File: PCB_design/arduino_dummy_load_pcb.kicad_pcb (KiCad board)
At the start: 2 copper layers, 122 parts, among them J1 Barrel_Jack, J2 Conn_02x08_Odd_Even, U1 MCP3208

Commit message: KiCad routing for the win!
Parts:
- removed the QB1 at (210.8, 87.6)
- moved BATT2 308.3 mm to (312.4, 160.0)
- moved RB4 212.4 mm to (266.6, 115.6)
- moved RB8 212.1 mm to (266.8, 125.7)
- moved DB2 207.4 mm to (273.9, 119.4)
- moved RB7 205.1 mm to (266.7, 120.7)
- moved BATT1 190.4 mm to (157.5, 142.2), turned to 270 degrees
- moved DB1 190.3 mm to (256.5, 114.3)
- moved DB4 190.3 mm to (256.5, 121.9)
- moved DB5 190.3 mm to (256.5, 124.5)
- moved RB5 183.1 mm to (248.9, 72.4)
- moved DB3 181.4 mm to (252.7, 103.8), turned to 90 degrees
- moved RB6 179.0 mm to (248.8, 77.5)
- moved RB3 170.5 mm to (248.8, 82.5)
- moved CB4 154.8 mm to (227.3, 96.5), turned to 90 degrees
- moved QA4 136.3 mm to (160.0, 106.7), turned to 180 degrees
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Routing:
- net GND: track 4.77 -> 160.5 mm
- net Net-(QA2-Pad3): track 0.00 -> 126.9 mm
- net Net-(QA3-Pad3): track 0.00 -> 115.0 mm
- net Net-(CA2-Pad1): track 10.3 -> 44.4 mm
- net I_OUT_A: track 0.00 -> 26.7 mm
- net Net-(QA2-Pad1): track 0.00 -> 24.2 mm
- net Net-(QA3-Pad1): track 0.00 -> 18.6 mm
- net Net-(DA1-Pad1): track 0.00 -> 18.5 mm
- net Net-(CA4-Pad1): track 0.00 -> 15.8 mm
- net Net-(CA3-Pad1): track 0.00 -> 14.6 mm
- net Net-(DA2-Pad1): track 0.00 -> 13.5 mm
- net /TEST-UNIT-A/STOP: track 0.00 -> 12.0 mm
- net VREF: track 10.4 -> 21.6 mm
- net +5V: track 21.2 -> 31.6 mm
- net Net-(DA3-Pad1): track 0.00 -> 5.63 mm
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
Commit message: nearly finished PCB layout and routing
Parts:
- removed BATT2: Battery_Cell, Library:18650
- removed CB1, CB2: 10uF, Capacitors_SMD:C_0805_HandSoldering
- removed CB3, CB4: 100nF, Capacitors_SMD:C_0805_HandSoldering
- removed DB1, DB2, DB3, DB4, DB5: D, Diodes_SMD:D_SOD-123
- removed QB1, QB4: IPP45P03P4L-11, TO_SOT_Packages_THT:TO-220-3_Vertical
- removed QB2, QB3: IRFZ44N, TO_SOT_Packages_THT:TO-220-3_Vertical
- removed R10, R11, R12, R13, R14, R8, R9, RB2, RB3, RB4, RB5, RB6, RB7, RB8: 47k, Resistors_SMD:R_0805_HandSoldering
- removed RB1: 50m, Resistors_SMD:R_2512_HandSoldering
- removed RB10, RB9: POT, Potentiometers:Potentiometer_Trimmer_ACP_CA6v_Horizontal_MountLS
- removed RB11: 10k, Resistors_SMD:R_0805_HandSoldering
- removed RSB1, RSB10, RSB11, RSB12, RSB13, RSB14, RSB15, RSB16, RSB17, RSB18, RSB19, RSB2, RSB20, RSB3, RSB4, RSB5, RSB6, RSB7, RSB8, RSB9: 10, Resistors_THT:R_Axial_DIN0617_L17.0mm_D6.0mm_P7.62mm_Vertical
- removed UB1: MCP73826, TO_SOT_Packages_SMD:SOT-23-6_Handsoldering
- removed UB2: LM324, Housings_SOIC:SOIC-14_3.9x8.7mm_Pitch1.27mm
- removed UB3, UB4, UB5: TMP36, TO_SOT_Packages_THT:TO-92_Inline_Wide
- RA10, RA9: footprint Potentiometers:Potentiometer_Trimmer_ACP_CA6v_Horizontal_MountLS -> Potentiometers:Potentiometer_Trimmer_VishaySpectrol_Econtrim-Type36M
- moved J1 88.8 mm to (64.5, 119.4)
- moved RA6 81.6 mm to (78.7, 128.2), turned to 270 degrees
- moved R3 69.3 mm to (73.7, 128.2), turned to 270 degrees
- moved UA5 68.7 mm to (143.5, 120.7), turned to 270 degrees
- moved RA3 65.7 mm to (76.2, 128.2), turned to 270 degrees
- moved R4 61.1 mm to (71.1, 128.2)
- moved DA4 61.0 mm to (141.0, 116.8), turned to 0 degrees
- moved R1 56.9 mm to (82.5, 92.7)
- moved R2 56.8 mm to (82.5, 95.2)
- moved R5 52.2 mm to (82.5, 102.9), turned to 0 degrees
- moved J2 50.6 mm to (74.9, 83.8), turned to 180 degrees
- moved R7 50.1 mm to (82.5, 97.8), turned to 0 degrees
- moved R6 44.7 mm to (82.6, 100.3), turned to 0 degrees
- moved U1 37.3 mm to (73.8, 101.8), turned to 180 degrees
- moved DA3 37.2 mm to (110.1, 111.8), turned to 180 degrees
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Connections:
- R4 pad 1: Net-(R3-Pad1) -> Net-(R4-Pad1)
- R4 pad 2: GND -> CELL_TEMP_A
- R5 pad 2: I_OUT_A -> BATT_B
- R6 pad 1: Net-(R5-Pad1) -> Net-(R6-Pad1)
- R6 pad 2: GND -> I_OUT_B
- R7 pad 2: CELL_TEMP_A -> CELL_TEMP_B
- U1 pad 2: Net-(R5-Pad1) -> I_OUT_A
- U1 pad 3: Net-(R7-Pad1) -> Net-(R4-Pad1)
- U1 pad 4: Net-(R10-Pad1) -> Net-(R5-Pad1)
- U1 pad 5: Net-(R11-Pad1) -> Net-(R6-Pad1)
- U1 pad 6: Net-(R13-Pad1) -> Net-(R7-Pad1)
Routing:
- net BATT_A: track 5.08 -> 146.5 mm
- net CELL_TEMP_A: track 0.00 -> 88.2 mm
- net CHARGE: track 5.72 -> 83.8 mm
- net +9V: track 0.00 -> 67.9 mm
- net Net-(QA3-Pad3): track 115.0 -> 171.5 mm
- net I_SET: track 3.96 -> 50.0 mm
- net Net-(QA2-Pad3): track 126.9 -> 168.4 mm
- net GND: track 160.5 -> 119.9 mm
- net Net-(CA2-Pad1): track 44.4 -> 81.6 mm
- net Net-(DA3-Pad1): track 5.63 -> 40.0 mm
- net Net-(DA3-Pad2): track 0.00 -> 30.1 mm
- net Net-(R4-Pad1): track 0.00 -> 25.7 mm
- net Net-(QB1-Pad3): track 15.4 -> 0.00 mm
- net Net-(R13-Pad1): track 13.4 -> 0.00 mm
- net Net-(R11-Pad1): track 13.0 -> 0.00 mm
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
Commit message: Finalized/finished PCB layout. Phew! Version 0.00. Hopefully it works (fingers crossed)!
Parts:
- removed R7: 47k, Resistors_SMD:R_0805_HandSoldering
- added BATT2: Battery_Cell, Library:18650, F.Cu at (255.3, 111.8)
- added CB1: 10uF, Capacitors_SMD:C_0805_HandSoldering, F.Cu at (247.7, 59.7)
- added CB2: 10uF, Capacitors_SMD:C_0805_HandSoldering, F.Cu at (254.0, 68.6)
- added CB3: 100nF, Capacitors_SMD:C_0805_HandSoldering, F.Cu at (218.6, 64.8)
- added CB4: 100nF, Capacitors_SMD:C_0805_HandSoldering, F.Cu at (213.7, 64.8)
- added DB1: D, Diodes_SMD:D_SOD-123, F.Cu at (210.6, 76.6)
- added DB2: D, Diodes_SMD:D_SOD-123, F.Cu at (219.3, 85.2)
- added DB3: D, Diodes_SMD:D_SOD-123, F.Cu at (213.0, 69.8)
- added DB4: D, Diodes_SMD:D_SOD-123, F.Cu at (243.8, 74.9)
- added DB5: D, Diodes_SMD:D_SOD-123, F.Cu at (220.4, 69.8)
- added QB1: IPP45P03P4L-11, TO_SOT_Packages_THT:TO-220-3_Vertical, F.Cu at (258.0, 64.3)
- added QB2: IRFZ44N, TO_SOT_Packages_THT:TO-220-3_Vertical, F.Cu at (191.8, 77.5)
- added QB3: IRFZ44N, TO_SOT_Packages_THT:TO-220-3_Vertical, F.Cu at (238.8, 77.5)
- added QB4: IPP45P03P4L-11, TO_SOT_Packages_THT:TO-220-3_Vertical, F.Cu at (257.8, 76.2)
- added RB1: 50m, Resistors_SMD:R_2512_HandSoldering, F.Cu at (244.2, 64.3)
- added RB10: POT, Potentiometers:Potentiometer_Trimmer_VishaySpectrol_Econtrim-Type36M, F.Cu at (214.6, 57.2)
- added RB11: 10k, Resistors_SMD:R_0805_HandSoldering, F.Cu at (217.0, 68.8)
- added RB2: 47k, Resistors_SMD:R_0805_HandSoldering, F.Cu at (252.7, 59.7)
- added RB3: 47k, Resistors_SMD:R_0805_HandSoldering, F.Cu at (179.1, 86.4)
- added RB4: 47k, Resistors_SMD:R_0805_HandSoldering, F.Cu at (215.9, 87.5)
- added RB5: 47k, Resistors_SMD:R_0805_HandSoldering, F.Cu at (210.6, 81.7)
- added RB6: 47k, Resistors_SMD:R_0805_HandSoldering, F.Cu at (181.6, 86.4)
- added RB7: 47k, Resistors_SMD:R_0805_HandSoldering, F.Cu at (224.9, 85.1)
- added RB8: 47k, Resistors_SMD:R_0805_HandSoldering, F.Cu at (226.0, 81.7)
- added RB9: POT, Potentiometers:Potentiometer_Trimmer_VishaySpectrol_Econtrim-Type36M, F.Cu at (223.5, 57.2)
- added REG1: REG, Library:LM2596_module, F.Cu at (79.3, 101.6)
- added RSB1: 10, Resistors_THT:R_Axial_DIN0617_L17.0mm_D6.0mm_P7.62mm_Vertical, F.Cu at (202.8, 130.7)
- added RSB10: 10, Resistors_THT:R_Axial_DIN0617_L17.0mm_D6.0mm_P7.62mm_Vertical, F.Cu at (215.5, 100.2)
- added RSB11: 10, Resistors_THT:R_Axial_DIN0617_L17.0mm_D6.0mm_P7.62mm_Vertical, F.Cu at (229.5, 130.7)
- added RSB12: 10, Resistors_THT:R_Axial_DIN0617_L17.0mm_D6.0mm_P7.62mm_Vertical, F.Cu at (229.5, 123.0)
- added RSB13: 10, Resistors_THT:R_Axial_DIN0617_L17.0mm_D6.0mm_P7.62mm_Vertical, F.Cu at (229.5, 115.4)
- added RSB14: 10, Resistors_THT:R_Axial_DIN0617_L17.0mm_D6.0mm_P7.62mm_Vertical, F.Cu at (229.5, 107.8)
- added RSB15: 10, Resistors_THT:R_Axial_DIN0617_L17.0mm_D6.0mm_P7.62mm_Vertical, F.Cu at (229.5, 100.2)
- added RSB16: 10, Resistors_THT:R_Axial_DIN0617_L17.0mm_D6.0mm_P7.62mm_Vertical, F.Cu at (242.2, 130.7)
- added RSB17: 10, Resistors_THT:R_Axial_DIN0617_L17.0mm_D6.0mm_P7.62mm_Vertical, F.Cu at (242.2, 123.0)
- added RSB18: 10, Resistors_THT:R_Axial_DIN0617_L17.0mm_D6.0mm_P7.62mm_Vertical, F.Cu at (242.2, 115.4)
- added RSB19: 10, Resistors_THT:R_Axial_DIN0617_L17.0mm_D6.0mm_P7.62mm_Vertical, F.Cu at (242.2, 107.8)
- added RSB2: 10, Resistors_THT:R_Axial_DIN0617_L17.0mm_D6.0mm_P7.62mm_Vertical, F.Cu at (202.8, 123.0)
- added RSB20: 10, Resistors_THT:R_Axial_DIN0617_L17.0mm_D6.0mm_P7.62mm_Vertical, F.Cu at (242.2, 100.2)
- added RSB3: 10, Resistors_THT:R_Axial_DIN0617_L17.0mm_D6.0mm_P7.62mm_Vertical, F.Cu at (202.8, 115.4)
- added RSB4: 10, Resistors_THT:R_Axial_DIN0617_L17.0mm_D6.0mm_P7.62mm_Vertical, F.Cu at (202.8, 107.8)
- added RSB5: 10, Resistors_THT:R_Axial_DIN0617_L17.0mm_D6.0mm_P7.62mm_Vertical, F.Cu at (202.8, 100.2)
- added RSB6: 10, Resistors_THT:R_Axial_DIN0617_L17.0mm_D6.0mm_P7.62mm_Vertical, F.Cu at (215.5, 130.7)
- added RSB7: 10, Resistors_THT:R_Axial_DIN0617_L17.0mm_D6.0mm_P7.62mm_Vertical, F.Cu at (215.5, 123.0)
- added RSB8: 10, Resistors_THT:R_Axial_DIN0617_L17.0mm_D6.0mm_P7.62mm_Vertical, F.Cu at (215.5, 115.4)
- added RSB9: 10, Resistors_THT:R_Axial_DIN0617_L17.0mm_D6.0mm_P7.62mm_Vertical, F.Cu at (215.5, 107.8)
- added UB1: MCP73826, TO_SOT_Packages_SMD:SOT-23-6_Handsoldering, F.Cu at (257.8, 58.3)
- added UB2: LM324, Housings_SOIC:SOIC-14_3.9x8.7mm_Pitch1.27mm, F.Cu at (218.3, 79.3)
- added UB3: TMP36, TO_SOT_Packages_THT:TO-92_Inline_Wide, F.Cu at (251.5, 114.3)
- added UB4: TMP36, TO_SOT_Packages_THT:TO-92_Inline_Wide, F.Cu at (185.4, 82.5)
- added UB5: TMP36, TO_SOT_Packages_THT:TO-92_Inline_Wide, F.Cu at (246.4, 78.7)
- moved J1 46.2 mm to (71.1, 73.7)
- moved C1 43.4 mm to (77.0, 64.5)
- moved C3 43.4 mm to (77.0, 59.4)
- moved C4 43.4 mm to (77.0, 56.8)
- moved CA1 43.4 mm to (156.2, 59.7)
- moved CA2 43.4 mm to (162.6, 68.6)
- moved CA3 43.4 mm to (127.2, 64.8)
- moved CA4 43.4 mm to (122.2, 64.8)
- moved DA2 43.4 mm to (127.9, 85.2)
- moved DA3 43.4 mm to (121.5, 69.8)
- moved DA4 43.4 mm to (152.4, 74.9)
- moved DA5 43.4 mm to (129.0, 69.8)
- moved QA1 43.4 mm to (166.6, 64.3)
- moved QA3 43.4 mm to (147.3, 77.5)
- moved QA4 43.4 mm to (166.4, 76.2)
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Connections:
- R6 pad 2: I_OUT_B -> CELL_TEMP_B
- U1 pad 5: Net-(R6-Pad1) -> I_OUT_B
- U1 pad 6: Net-(R7-Pad1) -> Net-(R6-Pad1)
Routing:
- net BATT_B: track 0.00 -> 253.2 mm
- net Net-(QB3-Pad3): track 0.00 -> 232.2 mm
- net Net-(QB2-Pad3): track 0.00 -> 222.3 mm
- net CELL_TEMP_B: track 0.00 -> 187.3 mm
- net CHARGE: track 83.8 -> 250.5 mm
- net +9V: track 67.9 -> 209.3 mm, vias 0 -> 2
- net I_OUT_B: track 0.00 -> 123.0 mm, vias 0 -> 2
- net I_SET: track 50.0 -> 169.4 mm
- net GND: track 119.9 -> 205.9 mm, vias 0 -> 19
- net Net-(CB2-Pad1): track 0.00 -> 81.6 mm
- net +5V: track 40.3 -> 118.6 mm, vias 0 -> 6
- net Net-(QA2-Pad3): track 168.4 -> 225.6 mm
- net Net-(QA3-Pad3): track 171.5 -> 226.5 mm
- net Net-(DB3-Pad1): track 0.00 -> 41.0 mm
- net Net-(DB3-Pad2): track 0.00 -> 33.0 mm
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- added copper zone on F.Cu, net +5V
- added copper zone on B.Cu, net GND
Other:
- board outline added: 209.6 x 109.2 mm

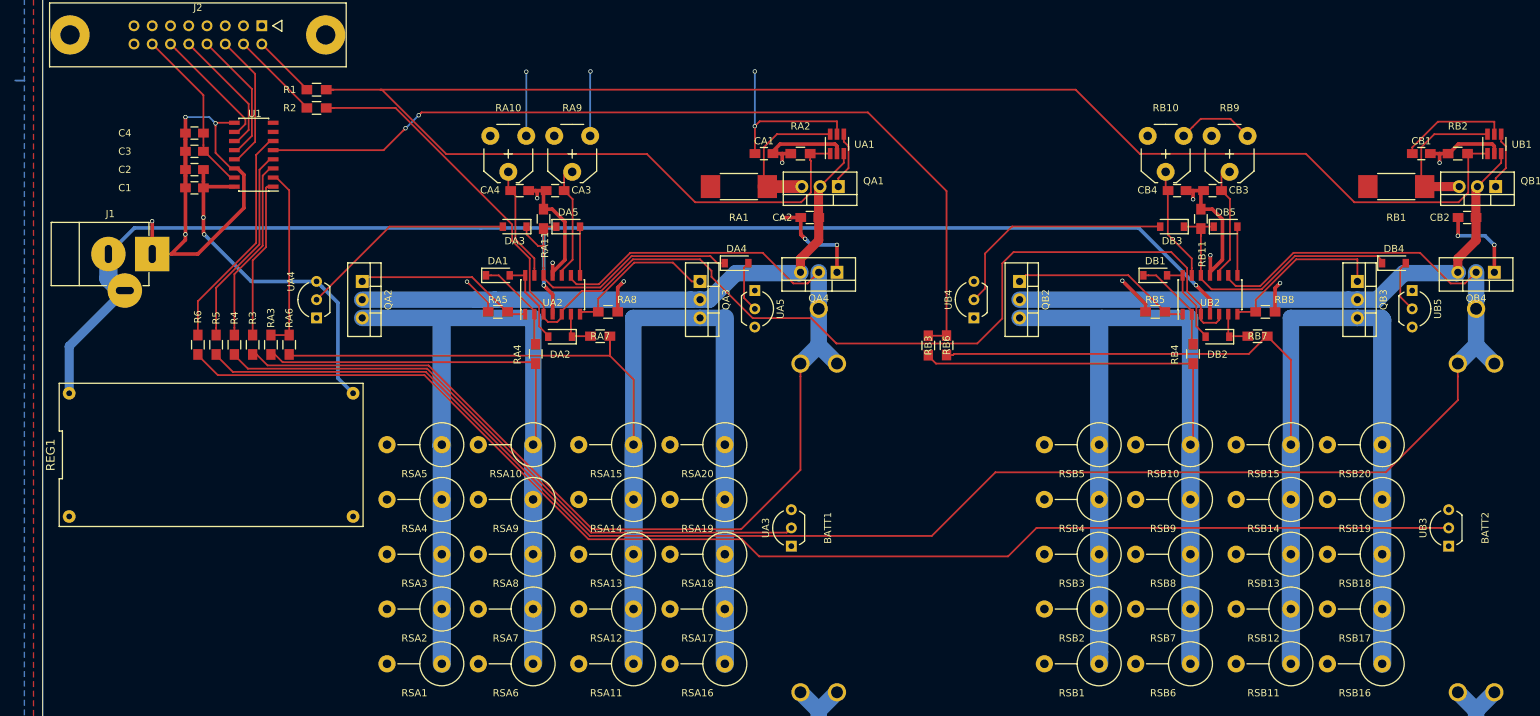
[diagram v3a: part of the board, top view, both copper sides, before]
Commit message: Resized vias in order to reduce potential showstoppers in DFM Checks
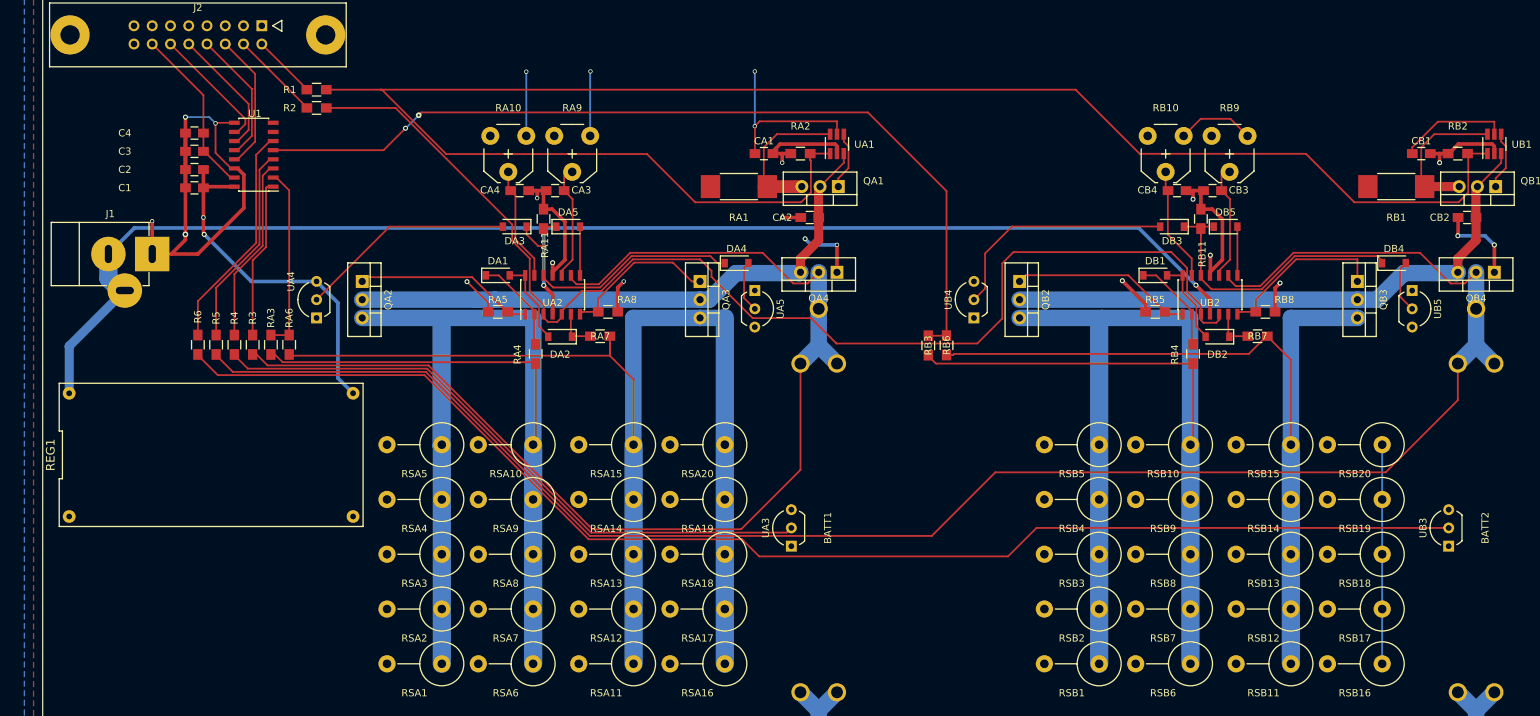
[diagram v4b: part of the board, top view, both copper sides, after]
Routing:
- net Net-(QB3-Pad3): track 232.2 -> 180.8 mm
- net +9V: track 209.3 -> 197.8 mm
- net GND: track 205.9 -> 202.4 mm
- net (no net): track 1.27 -> 0.00 mm
- net CHARGE: track 250.5 -> 249.5 mm
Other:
- net class Default: via_dia 0.6 -> 0.7
